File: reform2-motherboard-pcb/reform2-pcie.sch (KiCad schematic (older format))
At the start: 51 parts, among them J10 1-2199230-6, J11 48099-5701, U11 679105700, U20 AP22815, U23 IDT5V41066, Y3 25MHz

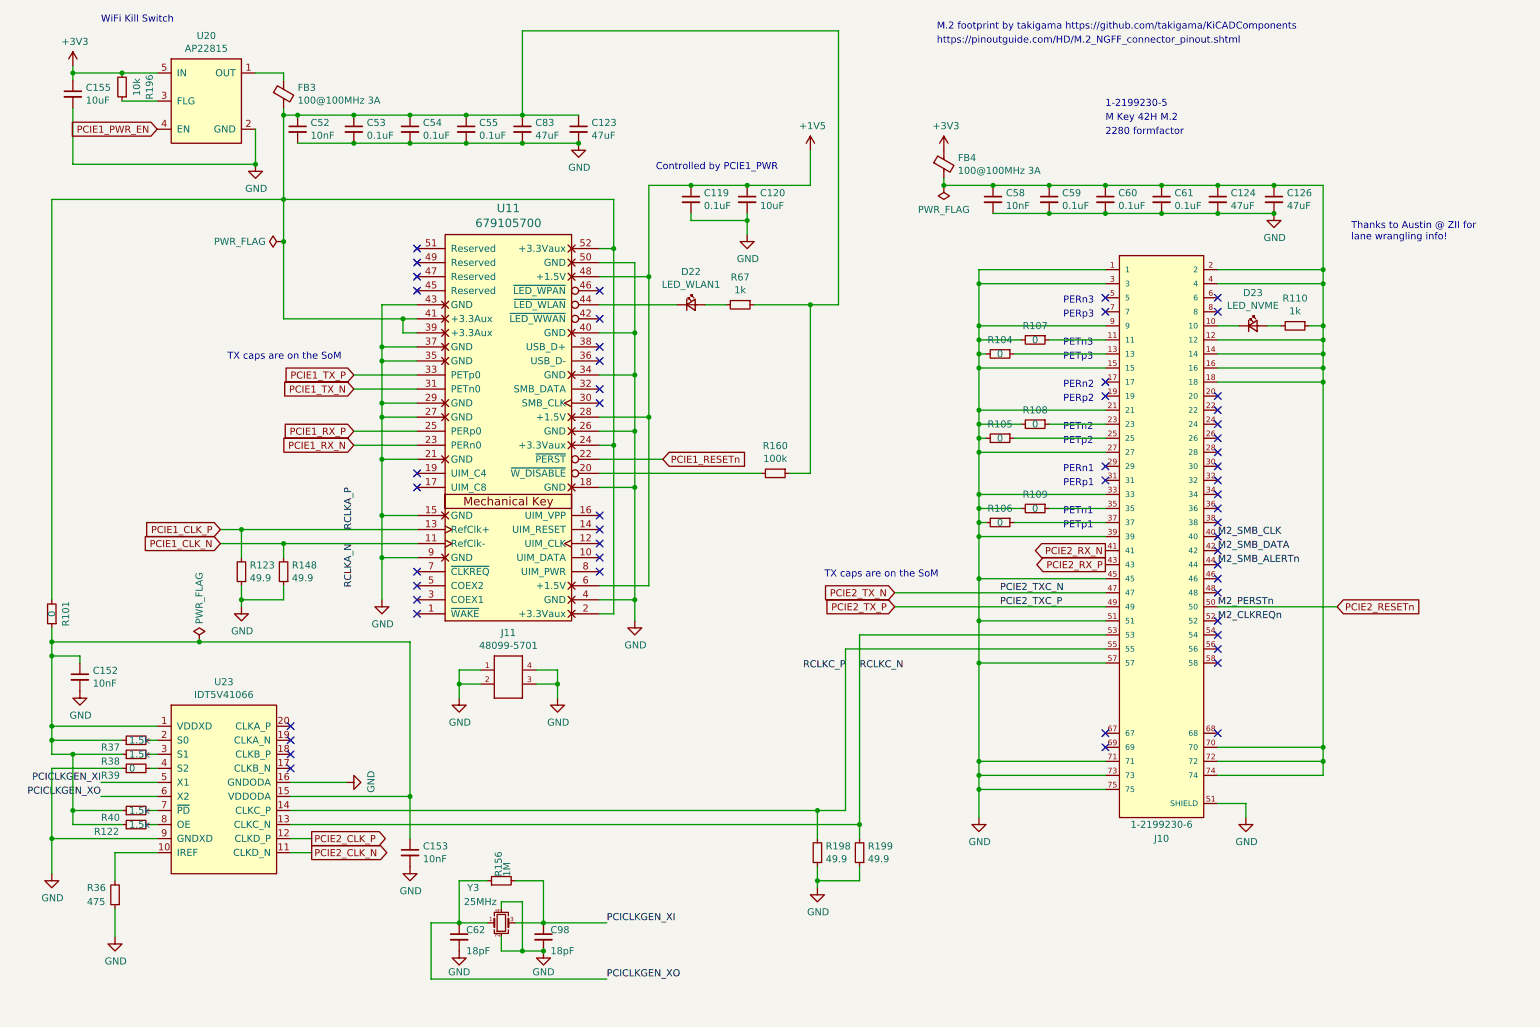
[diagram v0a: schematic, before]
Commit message: motherboard: add the split-up and cleaned up schematics that were made for the book
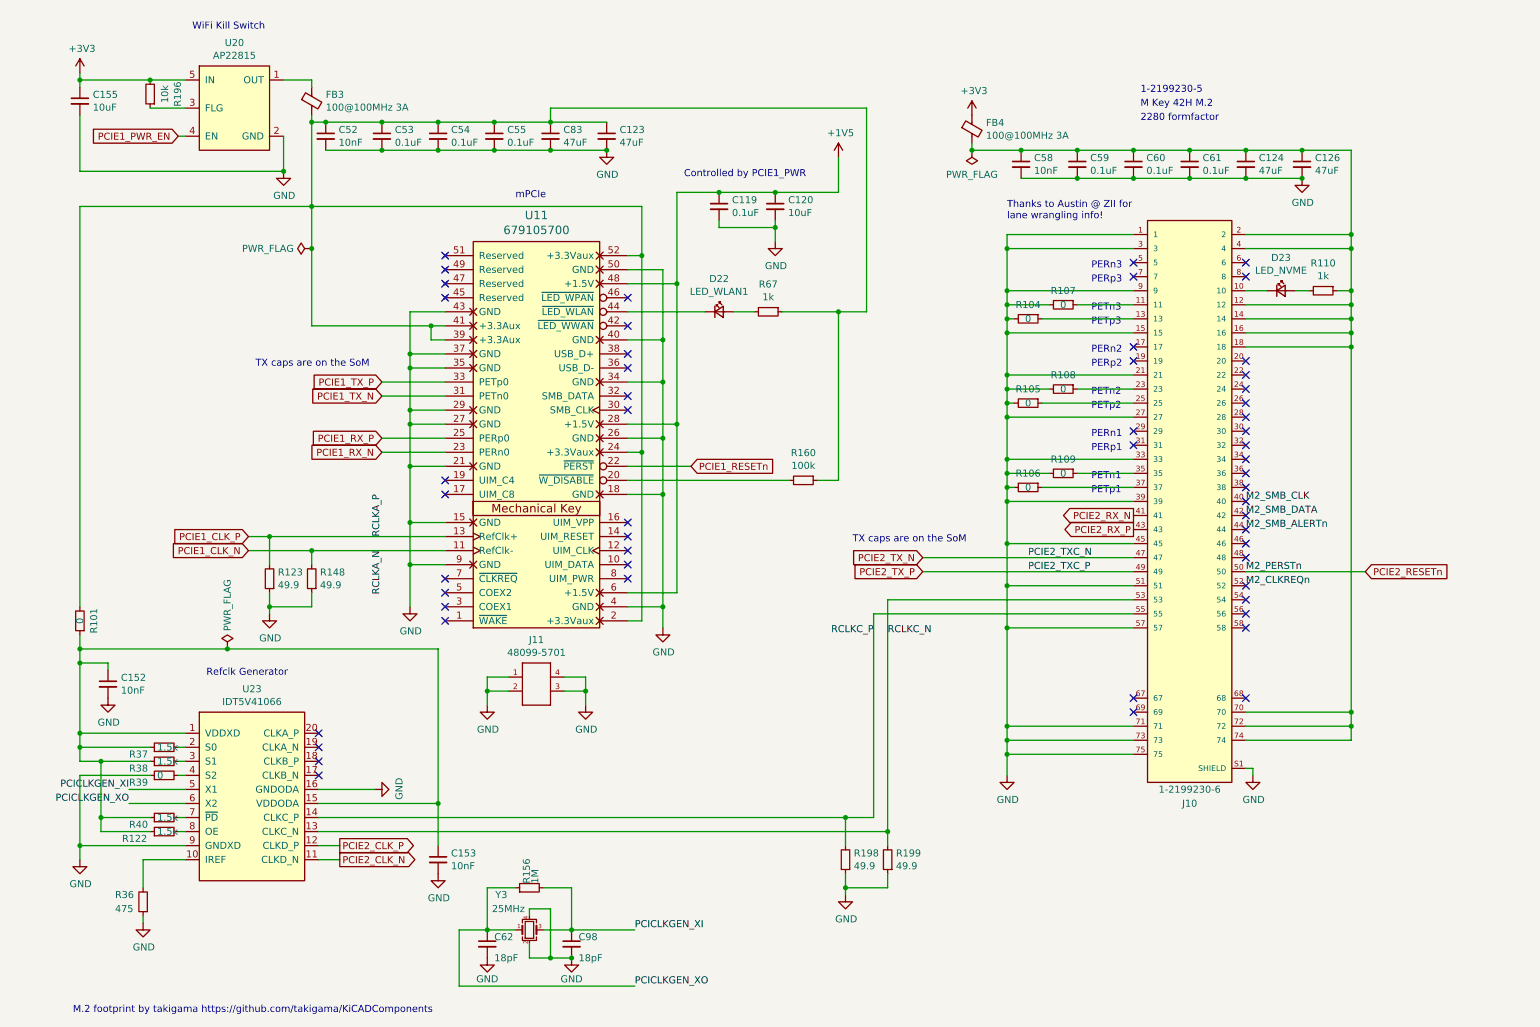
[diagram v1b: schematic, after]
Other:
- note added: "Refclk Generator"
- note added: "mPCIe"
- note removed: "https://pinoutguide.com/HD/M.2_NGFF_connector_pinout.shtml"
- moved on the sheet: C119, C120, C123, C124, C126, C152, C153, C155, C52, C53, C54, C55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
